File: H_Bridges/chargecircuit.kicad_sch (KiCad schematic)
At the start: 33 parts, among them J2 USB4085-GF-A_REVB, Q10 PMOS, Q9 PMOS, U2 max1898eub42+T, U3 TPS61023DRLR

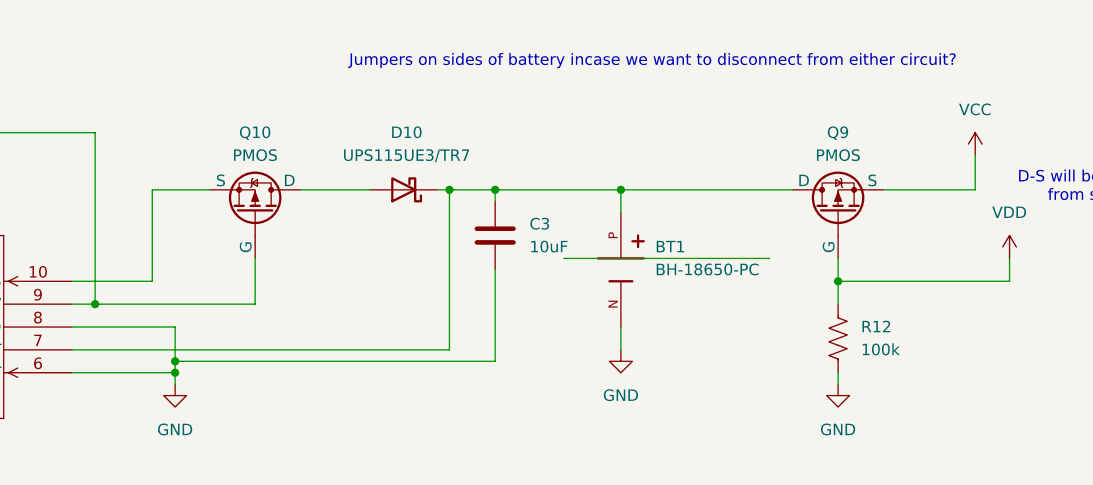
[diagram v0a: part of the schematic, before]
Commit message: added sim for H-bridge
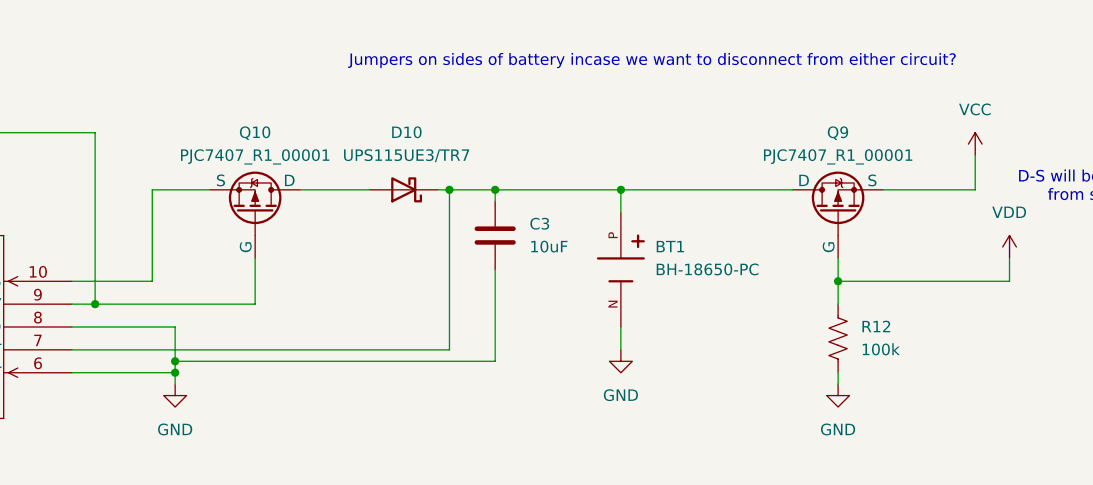
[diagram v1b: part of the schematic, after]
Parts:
- Q10, Q9: value PMOS -> PJC7407_R1_00001
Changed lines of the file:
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@@
 	(wire
 		(pts
-			(xy 196.85 45.72) (xy 219.71 45.72)
-		)
-		(stroke
-			(width 0)
-			(type default)
-		)
-	)
-	(wire
-		(pts
 			(xy 106.68 80.01) (xy 118.11 80.01)
 		)
@@
 			)
 		)
-		(property "Value" "PMOS"
+		(property "Value" "PJC7407_R1_00001"
 			(at 162.56 34.29 90)
 			(effects
@@
 			)
 		)
-		(property "Value" "PMOS"
+		(property "Value" "PJC7407_R1_00001"
 			(at 227.33 34.29 90)
 			(effects

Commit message: made final changes
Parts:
- removed D5: LED, LED_SMD:LED_0402_1005Metric_Pad0.77x0.64mm_HandSolder, symbol Device:LED
- added LED1: 553-0121F, 553-0121F_DIA, symbol 5530121F:553-0121F
- added R17: 300, Resistor_SMD:R_0603_1608Metric, symbol Device:R_US
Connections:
- net +5V: now also R17.2
- net GND: now also LED1.1
- net VDD: now also LED1.4
- net at U2.2 (*CHG): now also LED1.3
- new net: LED1.2, R17.1
